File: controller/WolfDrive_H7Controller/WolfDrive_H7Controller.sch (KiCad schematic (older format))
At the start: 281 parts, among them CN10 CONN_02X17, CN7 CONN_02X10, CN8 CONN_02X08, CN9 CONN_02X15, CON1 SD_Card, J1 USB_OTG, J10 GND, J11 GND, J12 5V, J13 Regen, J14 Throttle, J15 PWM1, J16 PWM2, J17 PWM3, J18 ~PWM1, J19 ~PWM2, J2 QSPI_CLK, J20 ~PWM3, J21 OCV, J22 ~F_C, J23 ~F_B, J24 ~F_A, J25 Overtemp, J26 PWM1, J27 Conn_01x04_Female, J29 Conn_01x04, J3 QSPI_NCS, J30 SPI2_SCK, J31 SPI2_NSS, J32 SPI2_MOSI, J33 SPI2_MISO, J34 PS-DIS, J35 3V3, J36 GND, J37 GND, J38 AGND, J39 SP1_MISO, J4 QSPI_IO0, J40 SP1_SCK, J41 SP1_NSS, J42 SP1_MOSI, J43 DB15_Female_HighDensity_Mount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, J5 QSPI_IO1, J6 QSPI_IO2, J7 QSPI_IO3, J8 12V, J9 GND, P10 GATE_IO_A, P11 GATE_IO_A, P7 CONN_01X02, P9 GATE_IO_A, Q2 Q_NMOS_DGS, U1 LM1117-5.0, U10 74LS136, U11 FT232RL, U2 LM1117-3.3, U3 MCP101-315D, U4 LTV-356T, U5 ISO7221, U7 OPA2340, U8 LM339, U9 CD4044B

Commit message: grounded test on FT232RL, issue #2
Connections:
- wire segments 922 -> 924
- no-connect marks 69 -> 68
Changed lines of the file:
@@
 	10950 4750 10950 4800
 Wire Wire Line
-	8550 4800 10550 4800
+	8550 4800 9950 4800
 Connection ~ 10950 4800
 Wire Wire Line
@@
 NoConn ~ 9950 3950
 NoConn ~ 9950 4150
-NoConn ~ 9950 4450
 NoConn ~ 11550 4450
 NoConn ~ 11550 4350
@@
 Wire Wire Line
 	2675 2100 2900 2100
+Wire Wire Line
+	9950 4450 9950 4800
+Connection ~ 9950 4800
+Wire Wire Line
+	9950 4800 10550 4800
 $EndSCHEMATC

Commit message: work towards fixing v0.1 issues, 1-5
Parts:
- removed D3, D4, D5: 3.3V, Diodes_SMD:D_SOD-523, symbol WolfDrive_H7Controller-rescue:WolfDrive_H7Controller-rescue_ZENER-RESCUE-WolfDr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
- removed J43: DB15_Female_HighDensity_MountingHoles, DriveParts:DB_15F-VGA-mountingholes, symbol conn:DB15_Female_HighDensity_MountingHoles
- removed Q2: Q_NMOS_DGS, w_smd_trans:sot23, symbol WolfDrive_H7Controller-rescue:device_Q_NMOS_DGS-RESCUE-WolfDrive_H7Controller-W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
- removed R42, R47, R48, R49, R50: 10k, Resistors_SMD:R_0603_HandSoldering, symbol WolfDrive_H7Controller-rescue:device_R-RESCUE-WolfDrive_H7Controller-WolfDrive_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
- removed R54: 240, Resistors_SMD:R_0805, symbol WolfDrive_H7Controller-rescue:device_R-RESCUE-WolfDrive_H7Controller-WolfDrive_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
- removed U1: LM1117-5.0, TO_SOT_Packages_SMD:TO-263-3_TabPin2, symbol regul:LM1117-5.0
- added C26, C46, C47, C48, C49, C50, C52, C65, C66, C68: 10n, Capacitors_SMD:C_0603_HandSoldering, symbol WolfDrive_H7Controller-rescue:device_C-RESCUE-WolfDrive_H7Controller-WolfDrive_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
- added D19, D20, D21, D22, D23, D3, D4, D5: SP0504BAHT, TO_SOT_Packages_SMD:TSOT-23-5, symbol Power_Protection:SP0504BAHT
- added D24: BAT54ADW, TO_SOT_Packages_SMD:SOT-363_SC-70-6_Handsoldering, symbol Diode:BAT54ADW
- added J28: GS3, Connectors:GS3, symbol Jumper:SolderJumper_3_Bridged12
- added J43, J44, J45, J46, J47, J48, J49, J50, J51, J52, J53, J54, J55, J56: GS3, Connectors:GS3, symbol Jumper:SolderJumper_3_Open
- added P1: GATE_IO_A, Connectors:IDC_Header_Straight_16pins, symbol Connector_Generic:Conn_02x08_Odd_Even
- added U1, U12, U13, U14, U15, U16, U17, U18, U19, U6: 74LVC1G02, TO_SOT_Packages_SMD:SOT-353_SC-70-5_Handsoldering, symbol 74xGxx:74LVC1G02
- added U20: 74HC266, Housings_SOIC:SOIC-14_3.9x8.7mm_Pitch1.27mm, symbol 4xxx:4077
- C7: footprint Capacitors_SMD:C_1210 -> Capacitors_SMD:C_1210_HandSoldering
- CN10: symbol WolfDrive_H7Controller-rescue:WolfDrive_H7Controller-rescue_CONN_02X17-RESCUE-WolfDrive_H7Controller-WolfDrive_H7Contro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 -> Connector_Generic:Conn_02x17_Odd_Even
- CN7: symbol WolfDrive_H7Controller-rescue:WolfDrive_H7Controller-rescue_CONN_02X10-RESCUE-WolfDrive_H7Controller-WolfDrive_H7Contro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 -> Connector_Generic:Conn_02x10_Odd_Even
- CN8, P10, P11, P9: symbol WolfDrive_H7Controller-rescue:WolfDrive_H7Controller-rescue_CONN_02X08-RESCUE-WolfDrive_H7Controller-WolfDrive_H7Contro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 -> Connector_Generic:Conn_02x08_Odd_Even
- CN9: symbol WolfDrive_H7Controller-rescue:WolfDrive_H7Controller-rescue_CONN_02X15-RESCUE-WolfDrive_H7Controller-WolfDrive_H7Contro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 -> Connector_Generic:Conn_02x15_Odd_Even
- D1: symbol WolfDrive_H7Controller-rescue:ESD_Protection_SP0503BAHT-RESCUE-WolfDrive_H7Controller-WolfDrive_H7Controller-rescue -> Power_Protection:SP0503BAHT
- FL1: symbol device:EMI_Filter_CommonMode -> Device:EMI_Filter_CommonMode
- I1, I2, I3: footprint SMD_Packages:SOIC-8-N -> Housings_SOIC:SOIC-8_3.9x4.9mm_Pitch1.27mm
- J1: symbol conn:USB_OTG -> Connector_Specialized:USB_OTG
- J10, J11, J13, J14, J15, J16, J17, J18, J19, J2, J20, J21, J22, J23, J24, J25, J3, J30, J31, J32, J33, J34, J35, J36, J37, J38, J39, J4, J40, J41, J42, J5, J6, J7, J8, J9: symbol conn:TEST_1P -> Connector_Specialized:Test_Point_Flag
- J12: value 5V -> 12VA; symbol conn:TEST_1P -> Connector_Specialized:Test_Point_Flag
- J26: value PWM1 -> PWM_EN; symbol conn:TEST_1P -> Connector_Specialized:Test_Point_Flag
- J27: symbol conn:Conn_01x04_Female -> Connector_Specialized:Conn_01x04_Female
- J29: symbol conn:Conn_01x04 -> Connector_Generic:Conn_01x04
- L1: symbol device:Ferrite_Bead -> Device:Ferrite_Bead
- L14, L15, L18, L9: footprint Inductors_NEOSID:Neosid_Inductor_SM-NE30_SMD1210 -> Inductors_NEOSID:Neosid_Inductor_SM-NE45_SMD1812
- MK1, MK2, MK3, MK4: symbol mechanical:Mounting_Hole_PAD -> Mechanical:Mounting_Hole_PAD
- MK5, MK6, MK7, MK8, MK9: symbol mechanical:Mounting_Hole -> Mechanical:Mounting_Hole
- R39, R40, R45, R46: value 10k -> 680
- R60, R61, R62, R63, R64, R65: footprint LEDs:LED_0603_HandSoldering -> Resistors_SMD:R_0603_HandSoldering; symbol device:R_Small -> Device:R_Small
- U10: value 74LS136 -> 74HC266; symbol WolfDrive_H7Controller-rescue:WolfDrive_H7Controller-rescue_74LS136-RESCUE-WolfDrive_H7Controller-WolfDrive_H7Controlle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 -> 4xxx:4077
- U11: symbol ftdi:FT232RL -> Interface_USB:FT232RL
- U2: symbol regul:LM1117-3.3 -> Regulator_Linear:LM1117-3.3
- U3: symbol Power_Management:MCP101-315D -> Power_Supervisor:MCP101-315D
- U7: symbol linear:OPA2340 -> Amplifier_Operational:OPA2340
- U9: value CD4044B -> CD4043B
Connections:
- net labels added: +12VA, 12V_thr, Fault_A+, Fault_A-, Fault_B+, Fault_B-, Fault_C+, Fault_C-, Fault_Gate_A, Fault_Gate_B, Fault_Gate_C, Fault_OCV
- net labels removed: 5V_thr, ~Fault_A+, ~Fault_A-, ~Fault_B+, ~Fault_B-, ~Fault_C+, ~Fault_C-, ~Fault_Gate_A, ~Fault_Gate_B, ~Fault_Gate_C, ~Fault_OCV
- wire segments 924 -> 1000
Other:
- note added: "DS90LV028A are rated for 3.3V supply, but schematic has 5V connected!\n\n @jonblissett\n Owner\njonblissett commented 8 hours ago\nCan use DS90C401 instead - 5V compatible part, but for new version use DS90LV027AQ-Q1 and supply with 3.3V.\n\nWhole 5V supply may no longer be required?"
- note added: "FOOTPRINT"
- note added: "Fault signals intentionally inverted for failsafe when unplugging"
- note added: "Pin 26 (TEST) on FT232RL should be connected to GND -> short to pin 25.\nDevice does not enumerate unless D1 (SP0503BAHT) is not populated."
- note added: "Protection diodes D1-D3 on over-temperature trips incorrect value and not required (DNP).\nMOSFET Q2 footprint pinout incorrect.\nCD4044B pinout incorrect - actually pinout for CD4043B so need to invert all fault inputs.\nFootprint for DB15 vertical instead of right angle?\nConnectors CN7-CNCN10 mirrored - connections to STM32 board do not match."
- note added: "Seems to be due to following comment in DS90LV028a datasheet:\n"The receiver also supports open, shorted and terminated (100 Ω) input fail-safe. The receiver output is HIGH for all fail-safe conditions.""
- note removed: "3.3V (")(-_-)(")"
- moved on the sheet: C44, C82, C85, D14, D15, D16, D7, L18, R41, R43, R44

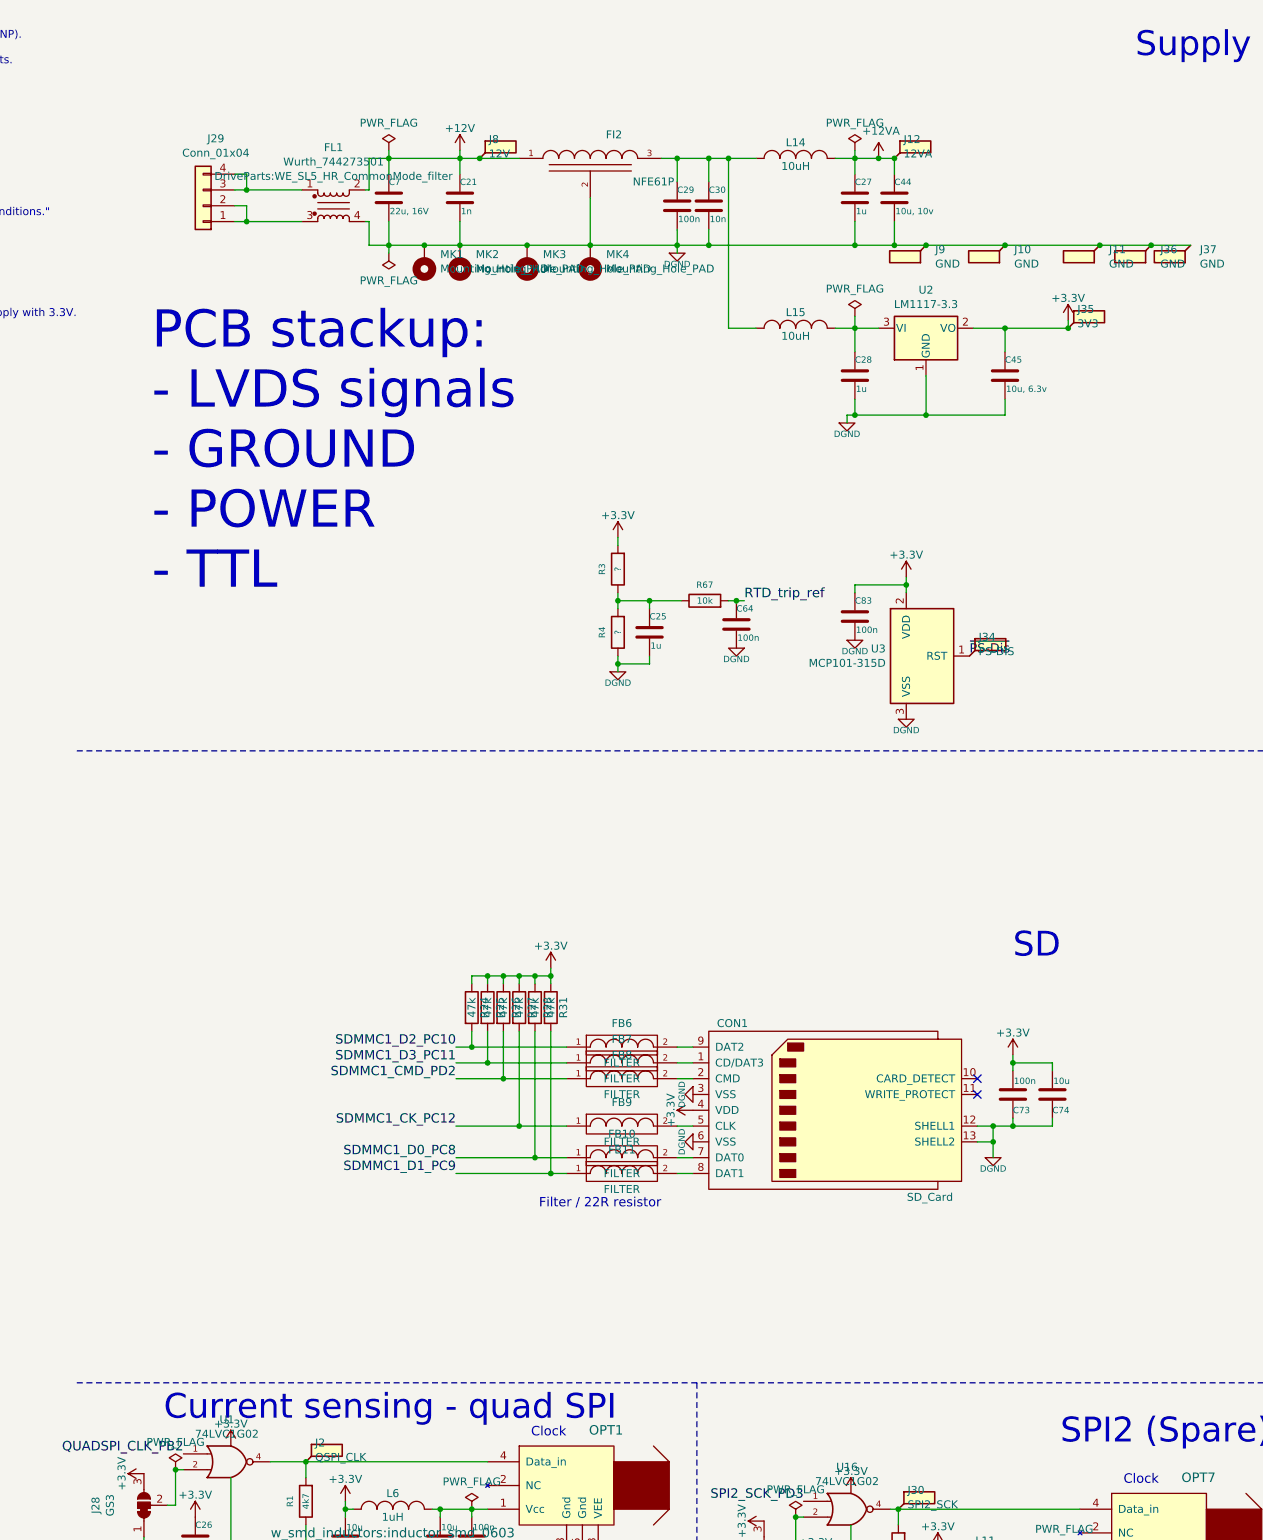
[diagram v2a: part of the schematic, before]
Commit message: Added input voltage protection
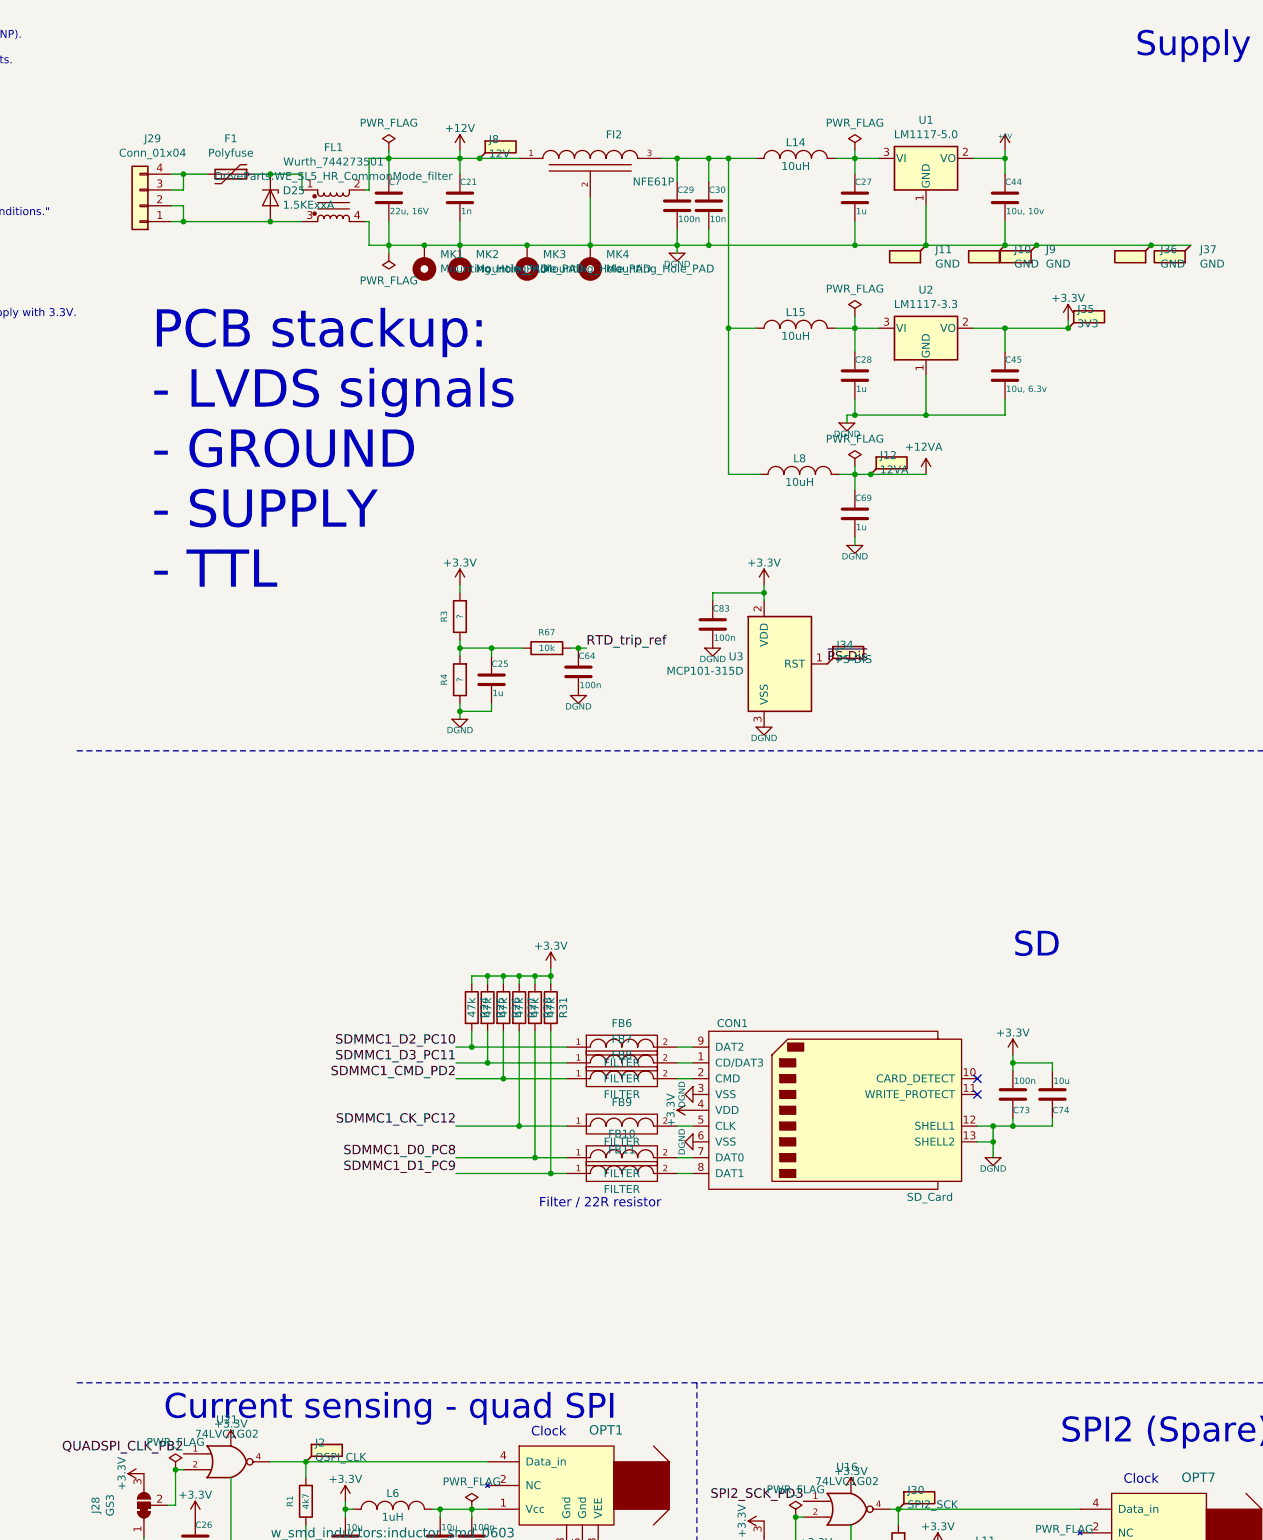
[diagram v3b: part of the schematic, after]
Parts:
- removed U1: 74LVC1G02, TO_SOT_Packages_SMD:SOT-353_SC-70-5_Handsoldering, symbol 74xGxx:74LVC1G02
- added C69: 1u, Capacitors_SMD:C_0603_HandSoldering, symbol WolfDrive_H7Controller-rescue:device_C-RESCUE-WolfDrive_H7Controller-WolfDrive_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
- added D25: 1.5KExxA, Diode_SMD:D_SMB-SMC_Universal_Handsoldering, symbol Diode:1.5KExxA
- added F1: Polyfuse, symbol Device:Polyfuse
- added L8: 10uH, Inductors_NEOSID:Neosid_Inductor_SM-NE45_SMD1812, symbol WolfDrive_H7Controller-rescue:WolfDrive_H7Controller-rescue_INDUCTOR_SMALL-RESC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
- added U1: LM1117-5.0, TO_SOT_Packages_SMD:TO-263-3_TabPin2, symbol Regulator_Linear:LM1117-5.0
- added U21: 74LVC1G02, TO_SOT_Packages_SMD:SOT-353_SC-70-5_Handsoldering, symbol 74xGxx:74LVC1G02
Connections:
- net +12VA: now also C69.1, L8.2; no longer C27.1, C44.1, L14.2
- net +3V3: now also U21.5 (VCC)
- net +5V: now also C44.1, U1.2 (VO)
- net DGND: now also C69.2, U1.1 (GND), U21.3 (GND)
- net QUADSPI_CLK_PB2: now also U21.1
- net at C29.1, C30.1, FI2.3 (VO)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: now also L8.1
- net at J2.1, OPT1.4 (Data_in), R1.2: now also U21.4
- net at J28.2 (C): now also U21.2
- net at J29.3 (Pin_3), J29.4 (Pin_4): now also F1.2; no longer FL1.1
- net at FL1.3, J29.1 (Pin_1), J29.2 (Pin_2): now also D25.2 (A2)
- new net: C27.1, L14.2, U1.3 (VI)
- new net: D25.1 (A1), F1.1, FL1.1
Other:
- note added: "PCB stackup:\n- LVDS signals\n- GROUND\n- SUPPLY\n- TTL"
- note removed: "PCB stackup:\n- LVDS signals\n- GROUND\n- POWER\n- TTL"
- moved on the sheet: C25, C44, C64, C83, J11, J12, J29, J34, J9, R3, R4, R67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
